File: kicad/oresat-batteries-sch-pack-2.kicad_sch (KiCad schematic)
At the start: 87 parts, among them Q11 SI7111EDN-T1-GE3, Q22 SQS484ENW-T1_GE3, Q24 PMV45ENR, Q25 PMV45ENR, Q26 PMV45ENR, Q27 PMV45ENR, Q30 SI7111EDN-T1-GE3, Q31 SI7111EDN-T1-GE3, Q32 NTR4101, Q33 NTR4101, Q34 SI7111EDN-T1-GE3, Q35 SI7111EDN-T1-GE3, Q36 SI7111EDN-T1-GE3, Q37 SI7111EDN-T1-GE3, U13 S-8209AAA-T8T1U, U14 S-8209AAA-T8T1U, U15 LTC4412, U16 LTC4412, U17 MAX17205G

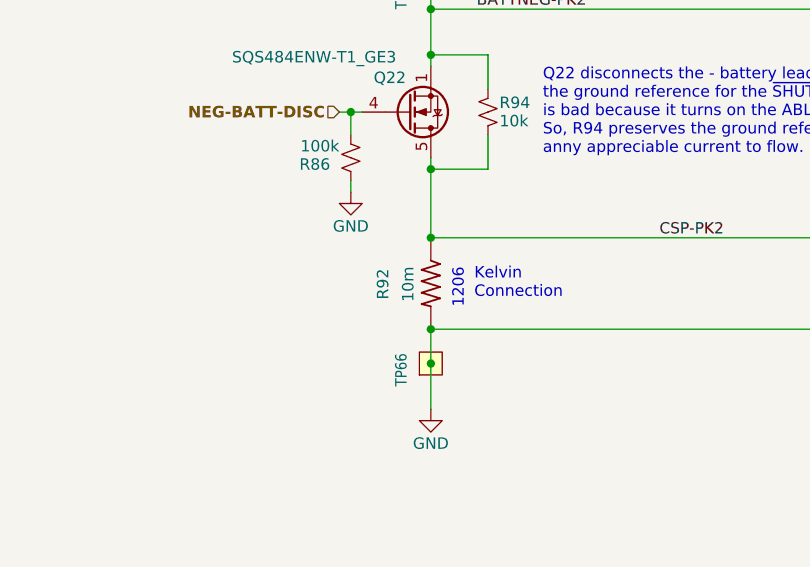
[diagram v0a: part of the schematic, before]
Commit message: Added MCXN. Preliminary power layout, started removal of old symbols and footprints.
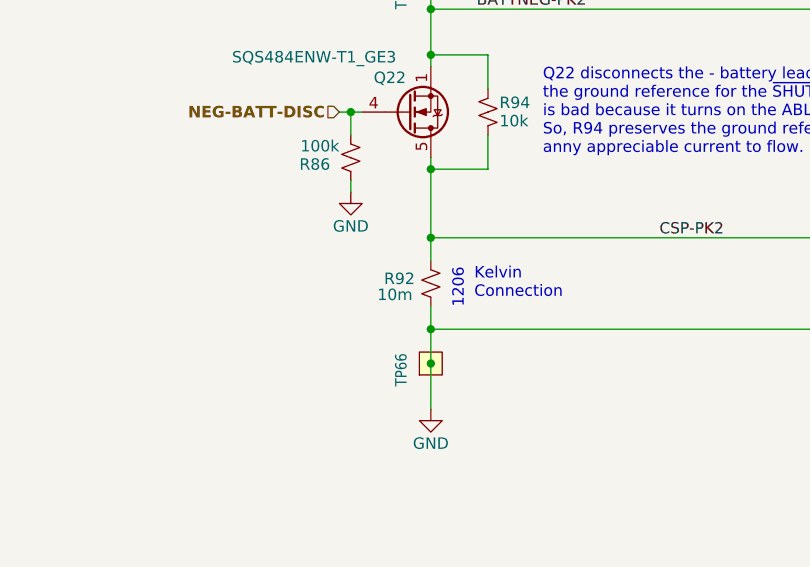
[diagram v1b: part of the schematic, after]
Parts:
- R92: symbol oresat-batteries-eagle-import:R-US_1206-C -> Device:R_Small_US
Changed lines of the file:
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@@
 	)
 	(junction
+		(at 259.08 241.3)
+		(diameter 0)
+		(color 0 0 0 0)
+	)
+	(junction
 		(at 259.08 168.91)
 		(diameter 0)
@@
 	)
 	(junction
+		(at 259.08 231.14)
+		(diameter 0)
+		(color 0 0 0 0)
+	)
+	(junction
 		(at 299.72 38.1)
 		(diameter 0)
@@
 	)
 	(junction
-		(at 259.08 231.14)
-		(diameter 0)
-		(color 0 0 0 0)
-	)
-	(junction
 		(at 259.08 128.27)
 		(diameter 0)
@@
 	)
 	(junction
-		(at 259.08 241.3)
-		(diameter 0)
-		(color 0 0 0 0)
-	)
-	(junction
 		(at 66.04 193.04)
 		(diameter 0)
@@
 	(wire
 		(pts
+			(xy 259.08 231.14) (xy 259.08 233.68)
+		)
+		(stroke
+			(width 0)
+			(type default)
+		)
+	)
+	(wire
+		(pts
 			(xy 250.19 166.37) (xy 175.26 166.37)
 		)
@@
 	(wire
 		(pts
+			(xy 259.08 238.76) (xy 259.08 241.3)
+		)
+		(stroke
+			(width 0)
+			(type default)
+		)
+	)
+	(wire
+		(pts
 			(xy 259.08 64.77) (xy 259.08 67.31)
 		)
@@
 	)
 	(symbol
-		(lib_id "oresat-batteries-eagle-import:R-US_1206-C")
-		(at 259.08 236.22 270)
+		(lib_id "Device:R_Small_US")
+		(at 259.08 236.22 0)
 		(unit 1)
 		(exclude_from_sim no)
@@
 		(dnp no)
 		(property "Reference" "R92"
-			(at 254.508 237.998 0)
+			(at 257.302 234.95 0)
 			(effects
 				(font
@@
 		)
 		(property "Value" "10m"
-			(at 257.302 238.252 0)
+			(at 257.048 236.728 0)
 			(effects
 				(font

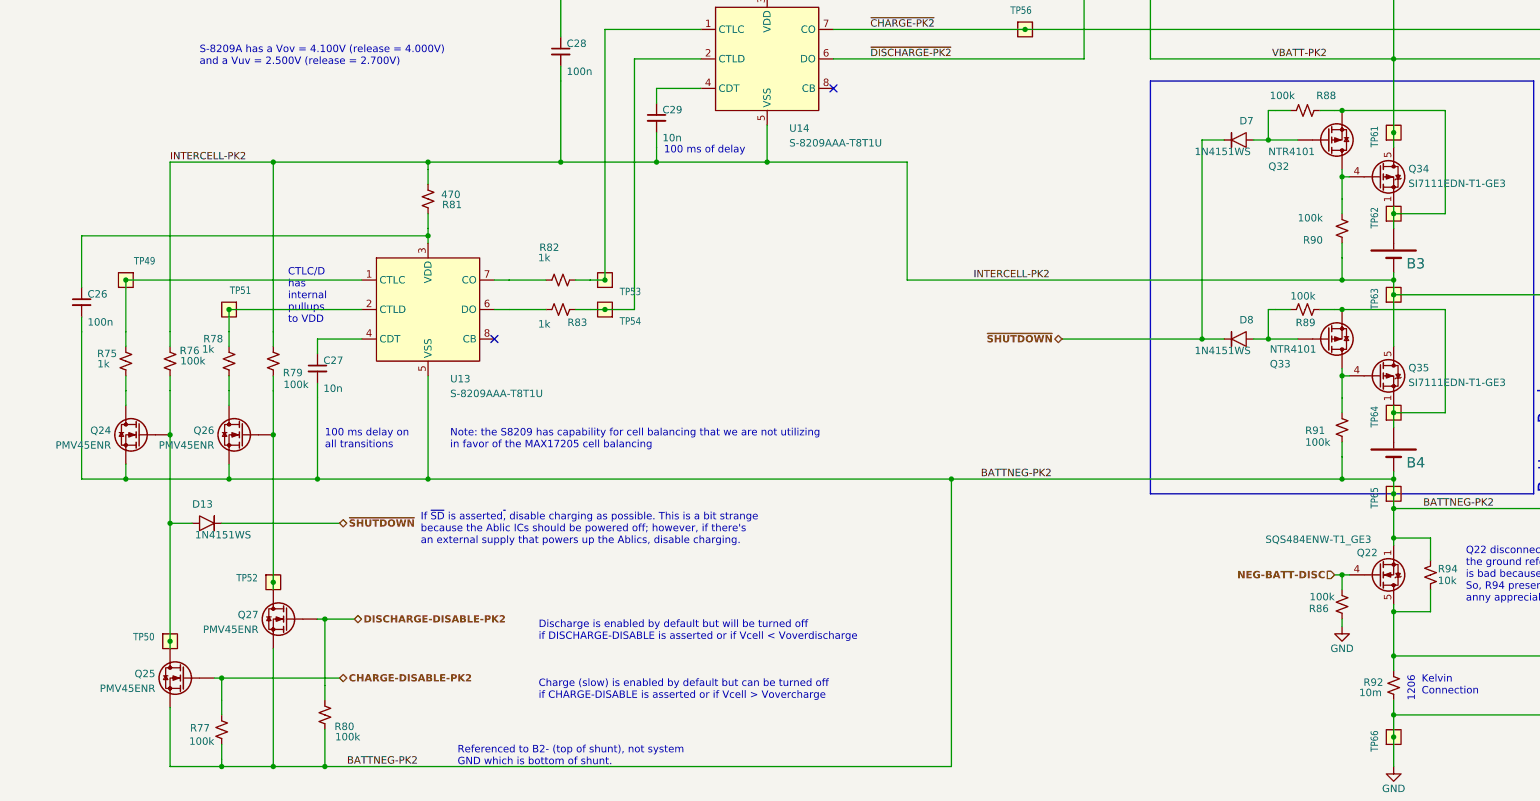
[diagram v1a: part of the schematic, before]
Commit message: Intermediary state on v4. Added one of two efuses.
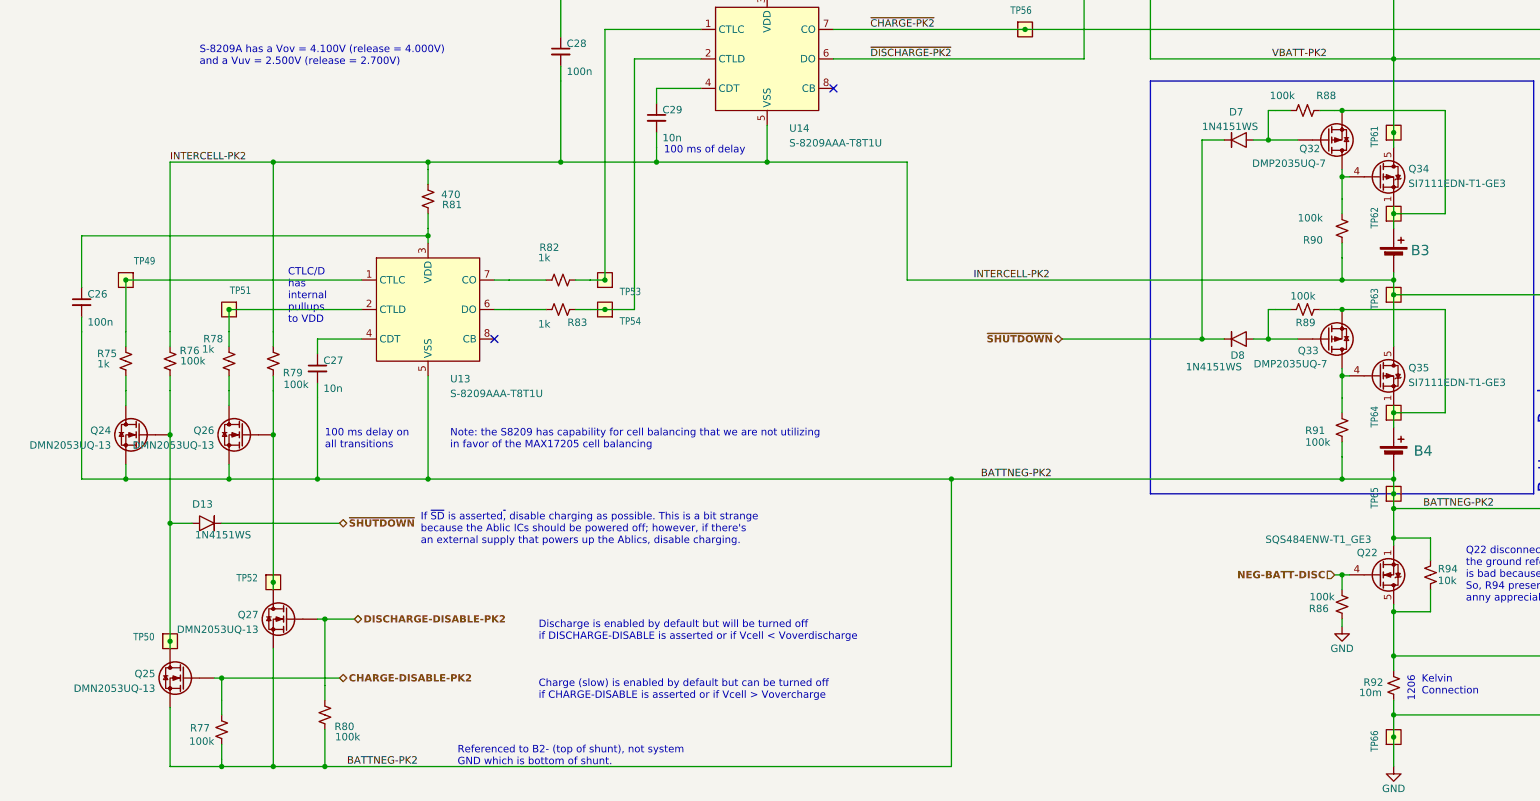
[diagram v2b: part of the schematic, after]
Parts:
- B3, B4: value B-18650-LI-BATTERY -> Tenergy 30005; symbol oresat-batteries-eagle-import:B-18650-LI-BATTERY -> Device:Battery_Cell
- Q24, Q25, Q26, Q27: value PMV45ENR -> DMN2053UQ-13; DPN 1727-2307-1-ND -> 31-DMN2053UQ-13CT-ND; MFR Nexperia -> Diodes Incorporated; MPN PMV45EN2R -> DMN2053UQ-13
- Q32, Q33: value NTR4101 -> DMP2035UQ-7; DPN NTR4101PT1GOSCT-ND -> 31-DMP2035UQ-7CT-ND; MFR ON Semi -> Diodes Incorporated; MPN NTR4101PT1G -> DMP2035UQ-7

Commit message: Schematic complete with new TPS circuit breaker; layout in progress
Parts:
- removed F2: 1206L500/12SLPR, oresat-passives:1206-C, symbol Device:Polyfuse_Small
- removed Q30: SI7111EDN-T1-GE3, Package_SO:Vishay_PowerPAK_1212-8_Single, symbol Transistor_FET:SiS443DN
- removed TP50, TP52: TEST-POINT-LARGE-SQUARE, oresat-misc:TestPoint-0.75mm-th, symbol oresat-misc:Test-Point-0.75mm-th
- removed U15: LTC4412, Package_TO_SOT_SMD:TSOT-23-6, symbol Power_Management:LTC4412xS6
- added C50, C61: 100n, oresat-passives:0603-C-NOSILK, symbol Device:C_Small
- added C62: 15n, oresat-passives:0603-C-NOSILK, symbol Device:C_Small
- added Q40: DMP2035UQ-7, Package_TO_SOT_SMD:SOT-23, symbol Transistor_FET:Q_PMOS_GSD
- added R110, R112: 210, oresat-passives:0603-C-NOSILK, symbol Device:R_Small_US
- added R116, R117, R118: 100k, oresat-passives:0603-C-NOSILK, symbol Device:R_Small_US
- added U15: TPS25983, oresat-ics:U-TPS259830LNRGER, symbol oresat-ics:TPS25983
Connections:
- net BATTNEG-PK2: no longer B4.2 (-), Q22.1 (S), Q22.2 (S), Q22.3 (S), R94.2, TP65.1
- net DCHG-STAT-OC-PK2: now also U15.13 (PG)
- net GND: now also C50.2, C61.2, C62.2, R110.2, R112.2, R117.1, U15.11 (NRETRY), U15.12 (OVLO), U15.[4,5,14,26] (GND)
- net VBATT-PK2: now also C30.1, Q40.2 (S), R118.2, U15.[1-3,16,25] (IN)
- net ~{DISCHARGE-PK2}: now also Q40.1 (G), R118.1; no longer R56.1
- net at R56.2: now also Q31.4 (G)
- net at Q31.5 (D), TP24.1: now also U15.[17-24] (OUT); no longer C30.1
- new net: C62.1, R56.1, U15.15 (DVDT/BGATE)
- new net: B4.2 (-), Q22.1 (S), Q22.2 (S), Q22.3 (S), R94.2, TP65.1
- new net: C61.1, U15.7 (ITIMER)
- new net: R116.1, R117.2, U15.6 (EN/UVLO)
- new net: C50.1, U15.10 (RETRY_DLY)
- new net: R110.1, U15.8 (ILIM)
- new net: R112.1, U15.9 (IMON)
- new net: Q40.3 (D), R116.2
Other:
- note added: "Cell UVLO/OVLO Control"
- note added: "Charge Control"
- note added: "Discharge Control"
- note added: "EFUSE Current limit: 7.1 A Voltage ramp up time: 24 ms Transient overcurrent timer: 2.0 ms Time between retries: 4.6 s"
- note added: "Off board on leads, thermally connected to battery cells"
- note added: "Retry Indefinitely"
- note added: "Retry every 4.7s"
- note removed: "Battery Pack w/shutdown"
- note removed: "CHARGE SWITCH"
- note removed: "DISCHARGE SWITCH"
- note removed: "PTC @ 5A"
- moved on the sheet: B3, B4, C11, C26, C27, C28, C29, C30, C31, C32, C33, C34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
